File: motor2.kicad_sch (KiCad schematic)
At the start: 2 parts, among them J2 motor, U2 DRV8835

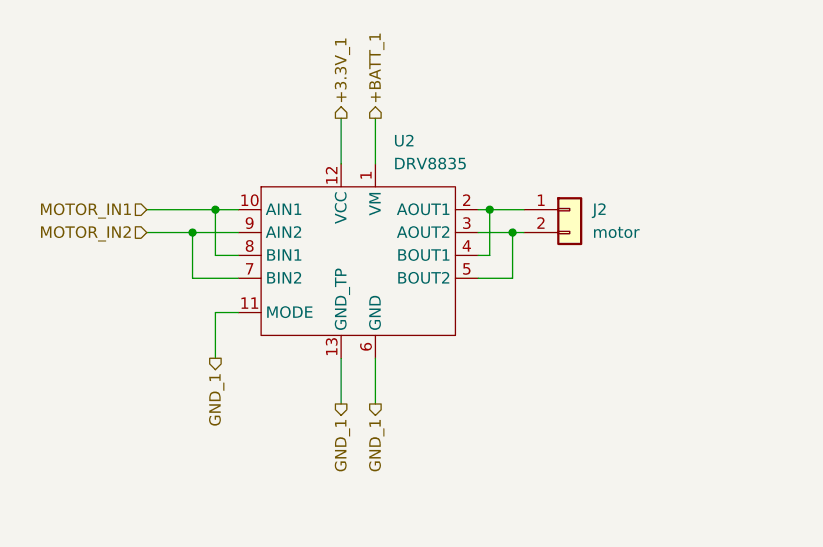
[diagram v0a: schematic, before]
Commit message: 部品配置完了
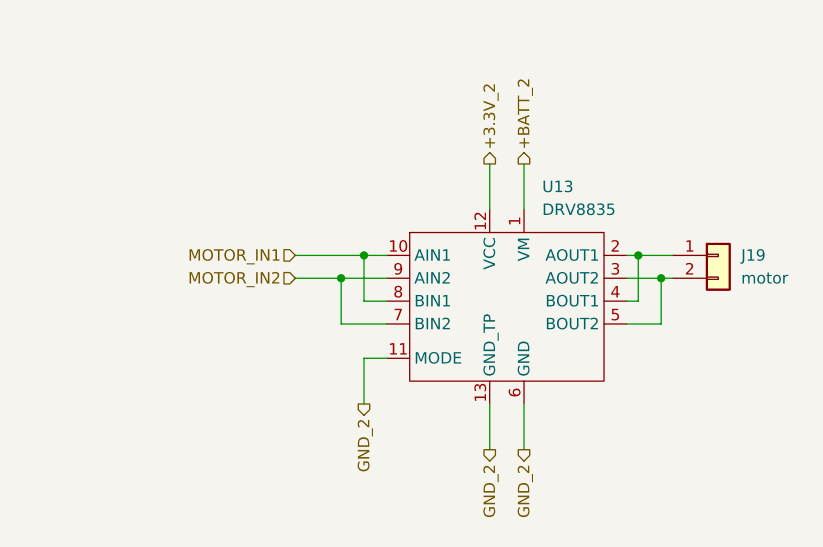
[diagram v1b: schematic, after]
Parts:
- removed J2: motor, Connector_PinSocket_1.27mm:PinSocket_1x02_P1.27mm_Vertical, symbol Connector_Generic:Conn_01x02
- removed U2: DRV8835, omni:DRV8835, symbol My_Device:DRV8835
- added J19: motor, Connector_PinSocket_1.27mm:PinSocket_1x02_P1.27mm_Vertical, symbol Connector_Generic:Conn_01x02
- added U13: DRV8835, omni:DRV8835, symbol My_Device:DRV8835
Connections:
- net MOTOR_IN1: now also U13.10 (AIN1), U13.8 (BIN1)
- net MOTOR_IN2: now also U13.7 (BIN2), U13.9 (AIN2)
- new net: J19.1 (Pin_1), U13.2 (AOUT1), U13.4 (BOUT1)
- new net: J19.2 (Pin_2), U13.3 (AOUT2), U13.5 (BOUT2)
- new net +3.3V_2: U13.12 (VCC)
- new net +BATT_2: U13.1 (VM)
- new net GND_2: U13.11 (MODE), U13.13 (GND_TP), U13.6 (GND)
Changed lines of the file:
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@@
 (kicad_sch (version 20211123) (generator eeschema)
   (paper "A4")
-  (junction (at 118.11 80.01) (diameter 0) (color 0 0 0 0)
+  (junction (at 132.08 87.63) (diameter 0) (color 0 0 0 0)
   )
-  (junction (at 115.57 82.55) (diameter 0) (color 0 0 0 0)
+  (junction (at 165.1 85.09) (diameter 0) (color 0 0 0 0)
   )
-  (junction (at 148.59 80.01) (diameter 0) (color 0 0 0 0)
+  (junction (at 167.64 87.63) (diameter 0) (color 0 0 0 0)
   )
-  (junction (at 151.13 82.55) (diameter 0) (color 0 0 0 0)
+  (junction (at 134.62 85.09) (diameter 0) (color 0 0 0 0)
   )
-  (wire (pts (xy 110.49 80.01) (xy 118.11 80.01))
+  (wire (pts (xy 127 85.09) (xy 134.62 85.09))
     (stroke (width 0) (type default) (color 0 0 0 0))
   )
-  (wire (pts (xy 118.11 80.01) (xy 120.65 80.01))
+  (wire (pts (xy 165.1 85.09) (xy 168.91 85.09))
     (stroke (width 0) (type default) (color 0 0 0 0))
   )
-  (wire (pts (xy 120.65 85.09) (xy 118.11 85.09))
+  (wire (pts (xy 137.16 90.17) (xy 134.62 90.17))
     (stroke (width 0) (type default) (color 0 0 0 0))
   )
-  (wire (pts (xy 135.89 69.85) (xy 135.89 74.93))
+  (wire (pts (xy 152.4 74.93) (xy 152.4 80.01))
     (stroke (width 0) (type default) (color 0 0 0 0))
   )
-  (wire (pts (xy 118.11 91.44) (xy 118.11 96.52))
+  (wire (pts (xy 167.64 87.63) (xy 168.91 87.63))
     (stroke (width 0) (type default) (color 0 0 0 0))
   )
-  (wire (pts (xy 132.08 96.52) (xy 132.08 101.6))
+  (wire (pts (xy 134.62 85.09) (xy 137.16 85.09))
     (stroke (width 0) (type default) (color 0 0 0 0))
   )
-  (wire (pts (xy 118.11 85.09) (xy 118.11 80.01))
+  (wire (pts (xy 163.83 87.63) (xy 167.64 87.63))
     (stroke (width 0) (type default) (color 0 0 0 0))
   )
-  (wire (pts (xy 120.65 91.44) (xy 118.11 91.44))
+  (wire (pts (xy 148.59 101.6) (xy 148.59 106.68))
     (stroke (width 0) (type default) (color 0 0 0 0))
   )
-  (wire (pts (xy 147.32 82.55) (xy 151.13 82.55))
+  (wire (pts (xy 165.1 90.17) (xy 165.1 85.09))
     (stroke (width 0) (type default) (color 0 0 0 0))
   )
-  (wire (pts (xy 115.57 87.63) (xy 115.57 82.55))
+  (wire (pts (xy 134.62 90.17) (xy 134.62 85.09))
     (stroke (width 0) (type default) (color 0 0 0 0))
   )
-  (wire (pts (xy 147.32 85.09) (xy 148.59 85.09))
+  (wire (pts (xy 167.64 87.63) (xy 167.64 92.71))
     (stroke (width 0) (type default) (color 0 0 0 0))
   )
-  (wire (pts (xy 151.13 82.55) (xy 152.4 82.55))
+  (wire (pts (xy 163.83 92.71) (xy 167.64 92.71))
     (stroke (width 0) (type default) (color 0 0 0 0))
   )
-  (wire (pts (xy 110.49 82.55) (xy 115.57 82.55))
+  (wire (pts (xy 134.62 96.52) (xy 134.62 101.6))
     (stroke (width 0) (type default) (color 0 0 0 0))
   )
-  (wire (pts (xy 147.32 80.01) (xy 148.59 80.01))
+  (wire (pts (xy 163.83 90.17) (xy 165.1 90.17))
     (stroke (width 0) (type default) (color 0 0 0 0))
   )
-  (wire (pts (xy 148.59 80.01) (xy 152.4 80.01))
+  (wire (pts (xy 132.08 92.71) (xy 132.08 87.63))
     (stroke (width 0) (type default) (color 0 0 0 0))
   )
-  (wire (pts (xy 135.89 96.52) (xy 135.89 101.6))
+  (wire (pts (xy 163.83 85.09) (xy 165.1 85.09))
     (stroke (width 0) (type default) (color 0 0 0 0))
   )
-  (wire (pts (xy 151.13 82.55) (xy 151.13 87.63))
+  (wire (pts (xy 137.16 92.71) (xy 132.08 92.71))
     (stroke (width 0) (type default) (color 0 0 0 0))
   )
-  (wire (pts (xy 120.65 87.63) (xy 115.57 87.63))
+  (wire (pts (xy 152.4 101.6) (xy 152.4 106.68))
     (stroke (width 0) (type default) (color 0 0 0 0))
   )
-  (wire (pts (xy 115.57 82.55) (xy 120.65 82.55))
+  (wire (pts (xy 132.08 87.63) (xy 137.16 87.63))
     (stroke (width 0) (type default) (color 0 0 0 0))
   )
-  (wire (pts (xy 148.59 85.09) (xy 148.59 80.01))
+  (wire (pts (xy 148.59 74.93) (xy 148.59 80.01))
     (stroke (width 0) (type default) (color 0 0 0 0))
   )
-  (wire (pts (xy 132.08 69.85) (xy 132.08 74.93))
+  (wire (pts (xy 137.16 96.52) (xy 134.62 96.52))
     (stroke (width 0) (type default) (color 0 0 0 0))
   )
-  (wire (pts (xy 147.32 87.63) (xy 151.13 87.63))
+  (wire (pts (xy 127 87.63) (xy 132.08 87.63))
     (stroke (width 0) (type default) (color 0 0 0 0))
   )
-  (hierarchical_label "+BATT_1" (shape output) (at 135.89 69.85 90)
+  (hierarchical_label "GND_2" (shape output) (at 134.62 101.6 270)
+    (effects (font (size 1.27 1.27)) (justify right))
+  )
+  (hierarchical_label "MOTOR_IN2" (shape input) (at 127 87.63 180)
+    (effects (font (size 1.27 1.27)) (justify right))
+  )
+  (hierarchical_label "GND_2" (shape output) (at 148.59 106.68 270)
+    (effects (font (size 1.27 1.27)) (justify right))
+  )
+  (hierarchical_label "MOTOR_IN1" (shape input) (at 127 85.09 180)
+    (effects (font (size 1.27 1.27)) (justify right))
+  )
+  (hierarchical_label "+BATT_2" (shape output) (at 152.4 74.93 90)
     (effects (font (size 1.27 1.27)) (justify left))
   )
-  (hierarchical_label "+3.3V_1" (shape output) (at 132.08 69.85 90)
+  (hierarchical_label "GND_2" (shape output) (at 152.4 106.68 270)
+    (effects (font (size 1.27 1.27)) (justify right))
+  )
+  (hierarchical_label "+3.3V_2" (shape output) (at 148.59 74.93 90)
     (effects (font (size 1.27 1.27)) (justify left))
   )
-  (hierarchical_label "MOTOR_IN1" (shape input) (at 110.49 80.01 180)
-    (effects (font (size 1.27 1.27)) (justify right))
-  )
-  (hierarchical_label "GND_1" (shape output) (at 135.89 101.6 270)
-    (effects (font (size 1.27 1.27)) (justify right))
-  )
-  (hierarchical_label "GND_1" (shape output) (at 132.08 101.6 270)
-    (effects (font (size 1.27 1.27)) (justify right))
-  )
-  (hierarchical_label "MOTOR_IN2" (shape input) (at 110.49 82.55 180)
-    (effects (font (size 1.27 1.27)) (justify right))
-  )
-  (hierarchical_label "GND_1" (shape output) (at 118.11 96.52 270)
-    (effects (font (size 1.27 1.27)) (justify right))
-  )
-  (symbol (lib_id "Connector_Generic:Conn_01x02") (at 157.48 80.01 0) (unit 1)
+  (symbol (lib_id "Connector_Generic:Conn_01x02") (at 173.99 85.09 0) (unit 1)
     (in_bom yes) (on_board yes) (fields_autoplaced)
-    (property "Reference" "J2" (id 0) (at 160.02 80.0099 0)
+    (property "Reference" "J19" (id 0) (at 176.53 85.0899 0)
       (effects (font (size 1.27 1.27)) (justify left))
     )
-    (property "Value" "motor" (id 1) (at 160.02 82.5499 0)
+    (property "Value" "motor" (id 1) (at 176.53 87.6299 0)
       (effects (font (size 1.27 1.27)) (justify left))
     )
-    (property "Footprint" "Connector_PinSocket_1.27mm:PinSocket_1x02_P1.27mm_Vertical" (id 2) (at 157.48 80.01 0)
+    (property "Footprint" "Connector_PinSocket_1.27mm:PinSocket_1x02_P1.27mm_Vertical" (id 2) (at 173.99 85.09 0)
       (effects (font (size 1.27 1.27)) hide)
     )
-    (property "Datasheet" "~" (id 3) (at 157.48 80.01 0)
+    (property "Datasheet" "~" (id 3) (at 173.99 85.09 0)
       (effects (font (size 1.27 1.27)) hide)
     )
@@
     (pin "2")
   )
-  (symbol (lib_id "My_Device:DRV8835") (at 133.35 66.04 0) (unit 1)
+  (symbol (lib_id "My_Device:DRV8835") (at 149.86 71.12 0) (unit 1)
     (in_bom yes) (on_board yes) (fields_autoplaced)
-    (property "Reference" "U2" (id 0) (at 137.9094 72.39 0)
+    (property "Reference" "U13" (id 0) (at 154.4194 77.47 0)
       (effects (font (size 1.27 1.27)) (justify left))
     )
-    (property "Value" "DRV8835" (id 1) (at 137.9094 74.93 0)
+    (property "Value" "DRV8835" (id 1) (at 154.4194 80.01 0)
       (effects (font (size 1.27 1.27)) (justify left))
     )
-    (property "Footprint" "omni:DRV8835" (id 2) (at 133.35 66.04 0)
+    (property "Footprint" "omni:DRV8835" (id 2) (at 149.86 71.12 0)
       (effects (font (size 1.27 1.27)) hide)
     )
-    (property "Datasheet" "" (id 3) (at 133.35 66.04 0)
+    (property "Datasheet" "" (id 3) (at 149.86 71.12 0)
       (effects (font (size 1.27 1.27)) hide)
     )
